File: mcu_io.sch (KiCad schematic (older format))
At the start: 36 parts

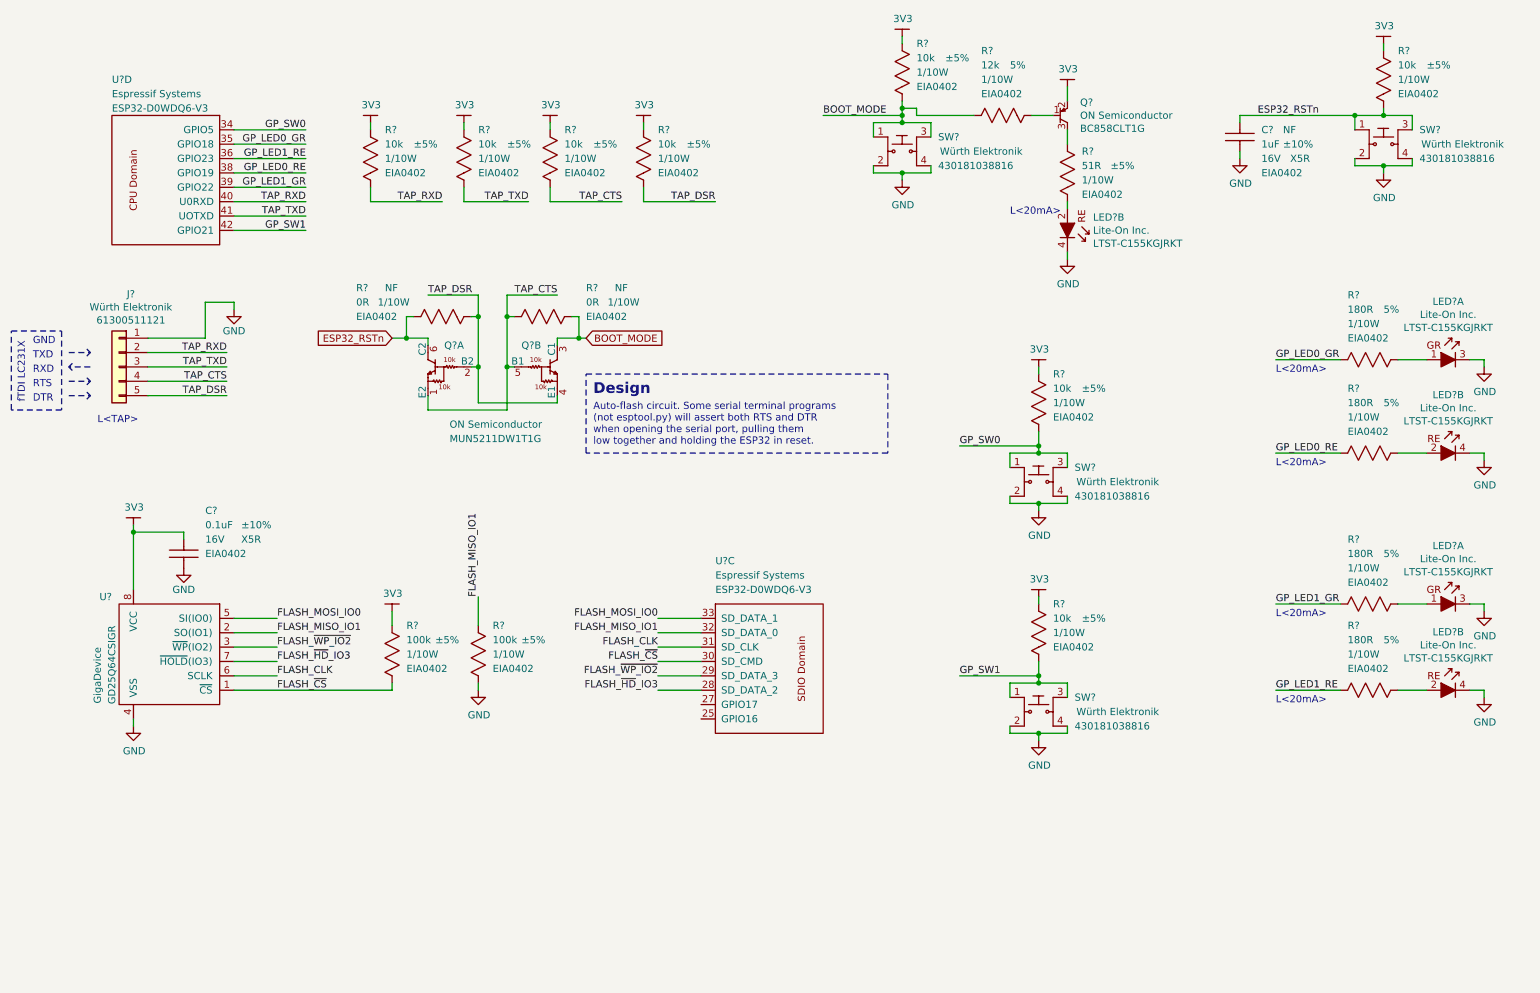
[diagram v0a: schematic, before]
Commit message: Bring out on headers all unused ESP32 pins.
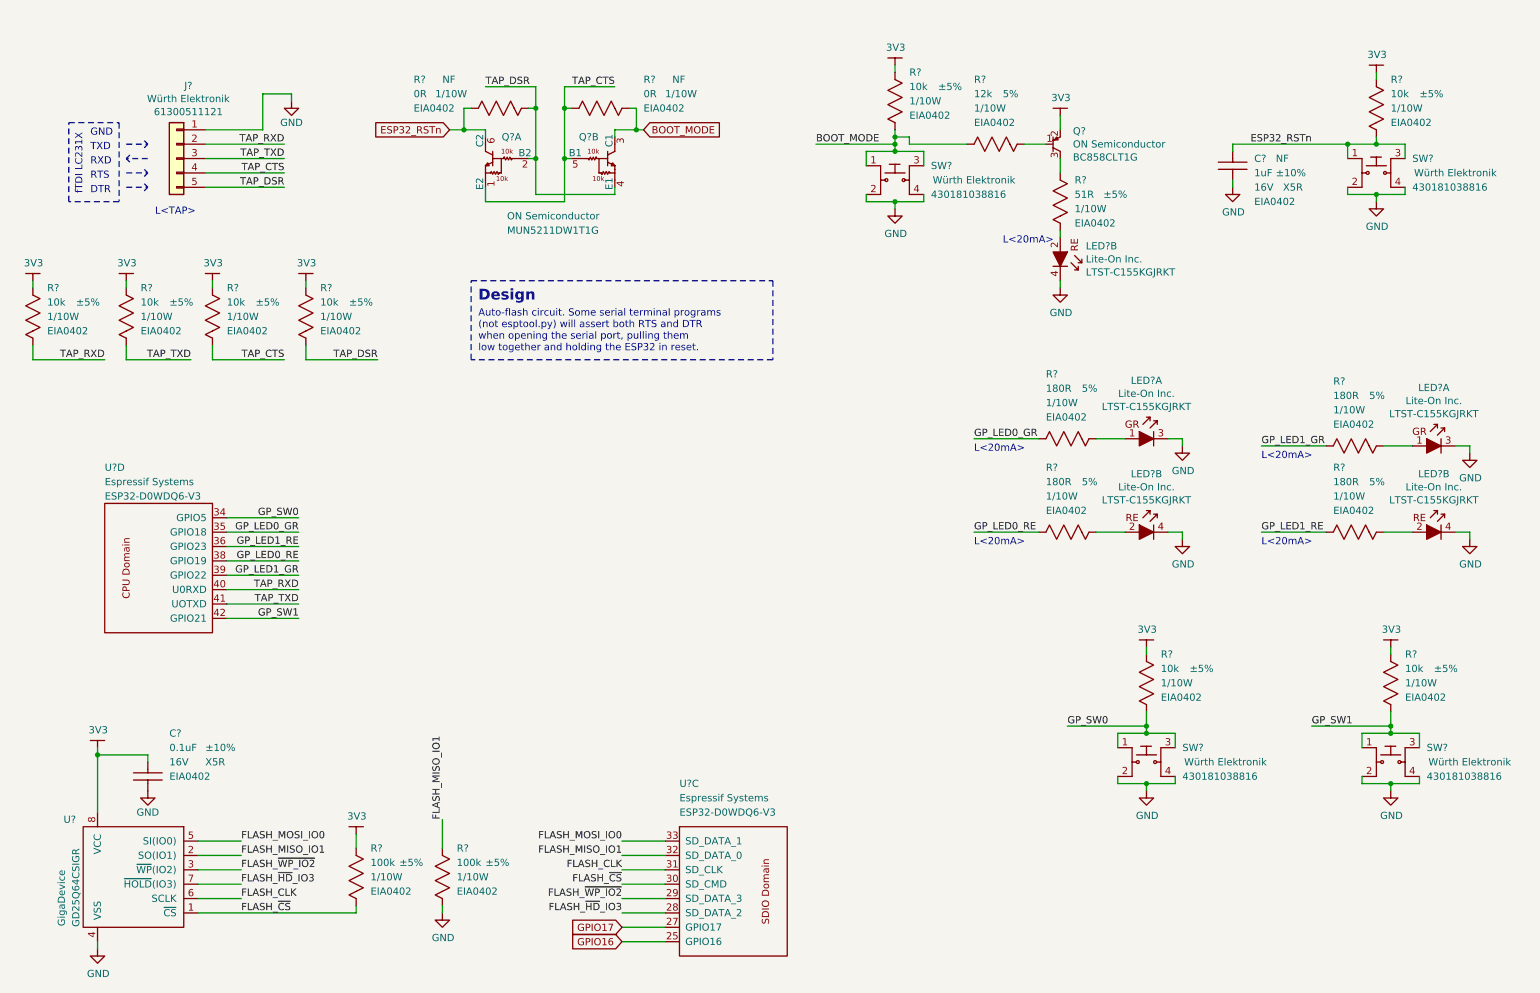
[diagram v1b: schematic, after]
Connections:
- net GPIO16: now reaches U?.25 (GPIO16)
- net GPIO17: now reaches U?.27 (GPIO17)
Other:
- moved on the sheet: C?, J?, LED?A, LED?B, Q?, Q?A, Q?B, R?, SW?, U?, U?C, U?D

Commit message: Annotate schematic.
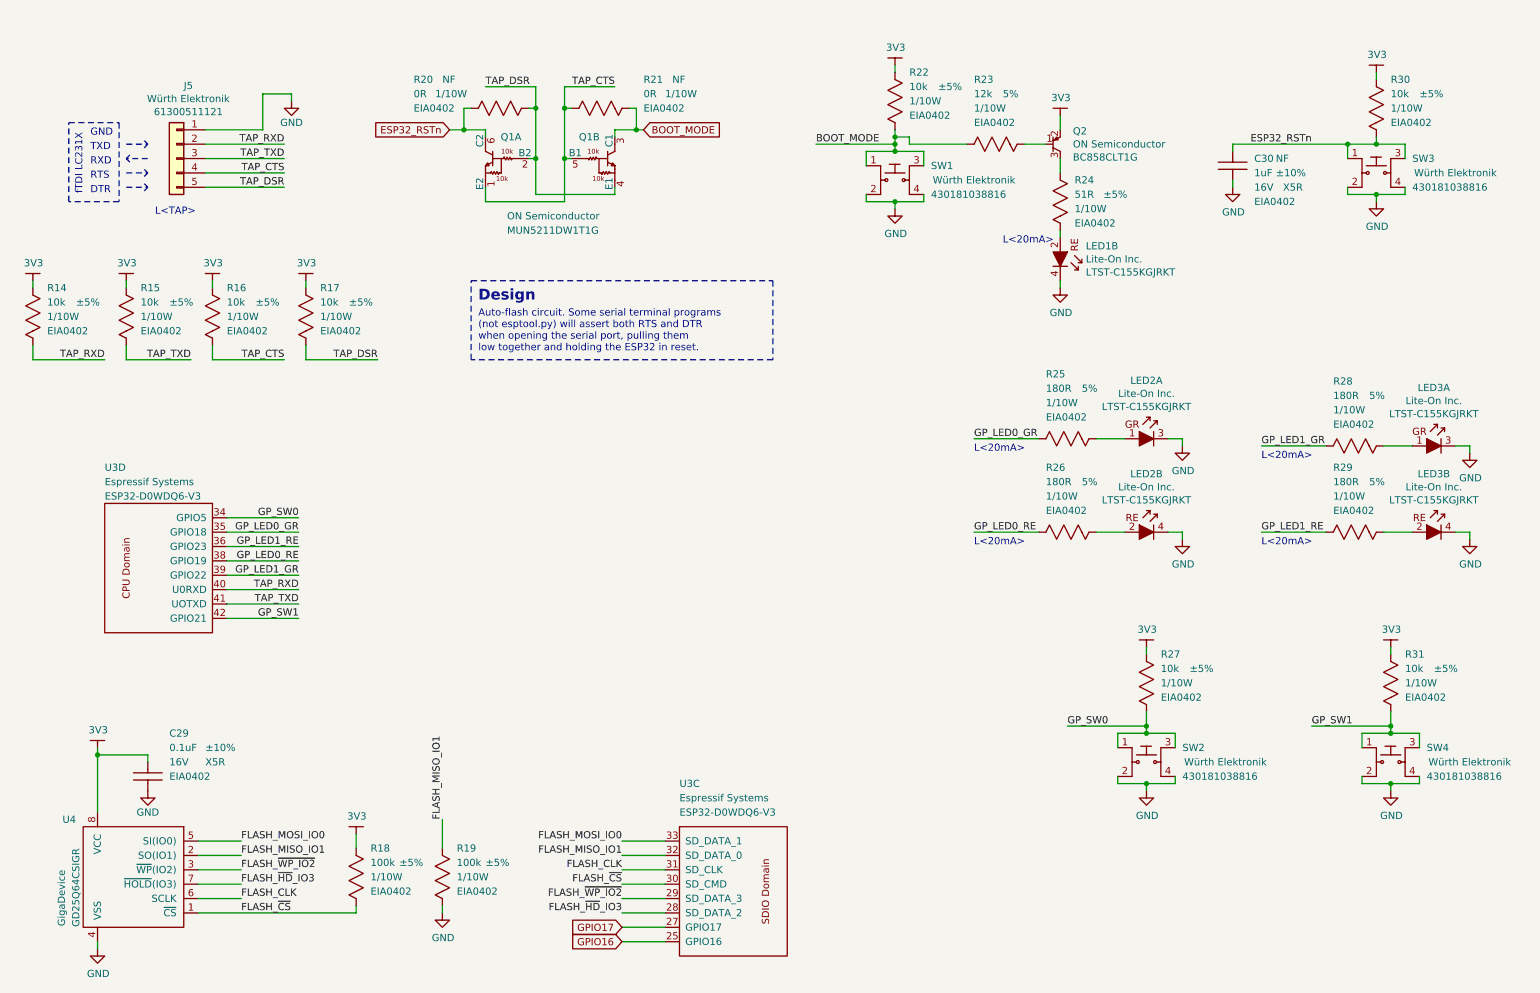
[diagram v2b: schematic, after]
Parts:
- gave numbers to parts that had none: 32
